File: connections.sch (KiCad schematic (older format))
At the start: 1 part

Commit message: Updated the schematic with some BUSes
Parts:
- added uUSB?: MICROUSB, symbol MICROUSB
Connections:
- net labels added: +5V, GNDPWR, USB0_0, USB0_1, USB0_2, eth0_0, eth0_1, eth0_10, eth0_2, eth0_3, eth0_4, eth0_5, eth0_6, eth0_7, eth0_8, eth0_9
- wire segments 0 -> 14
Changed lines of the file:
@@
-EESchema Schematic File Version 2  date 9/17/2011 12:57:37 AM
+EESchema Schematic File Version 2  date 9/17/2011 1:33:24 AM
 LIBS:power
 LIBS:device
@@
 LIBS:valves
 LIBS:rrae
+LIBS:connections-cache
 EELAYER 25  0
 EELAYER END
@@
 $EndDescr
 $Comp
+L GNDPWR #PWR?
+U 1 1 4E743F0C
+P 9800 2100
+F 0 "#PWR?" H 9800 2150 40  0001 C CNN
+F 1 "GNDPWR" H 9800 2020 40  0000 C CNN
+	1    9800 2100
+	1    0    0    -1
+$EndComp
+Wire Bus Line
+	7750 2100 7750 1100
+Wire Bus Line
+	5000 1800 5000 1600
+Wire Wire Line
+	5550 1700 5100 1700
+Wire Wire Line
+	5550 1800 5100 1800
+Wire Wire Line
+	5550 1900 5100 1900
+Wire Wire Line
+	8100 1200 7850 1200
+Wire Wire Line
+	8100 1300 7850 1300
+Wire Wire Line
+	8100 1400 7850 1400
+Wire Wire Line
+	8100 1500 7850 1500
+Wire Wire Line
+	8100 1600 7850 1600
+Wire Wire Line
+	8100 1700 7850 1700
+Wire Wire Line
+	8100 1800 7850 1800
+Wire Wire Line
+	8100 1900 7850 1900
+Wire Wire Line
+	8100 2000 7850 2000
+Wire Wire Line
+	8100 2100 7850 2100
+Wire Wire Line
+	8100 2200 7850 2200
+Entry Wire Line
+	7750 2100 7850 2200
+Entry Wire Line
+	7750 2000 7850 2100
+Entry Wire Line
+	7750 1900 7850 2000
+Entry Wire Line
+	7750 1800 7850 1900
+Entry Wire Line
+	7750 1700 7850 1800
+Entry Wire Line
+	7750 1600 7850 1700
+Entry Wire Line
+	7750 1500 7850 1600
+Entry Wire Line
+	7750 1400 7850 1500
+Entry Wire Line
+	7750 1300 7850 1400
+Entry Wire Line
+	7750 1200 7850 1300
+Entry Wire Line
+	7750 1100 7850 1200
+Text Label 7850 2200 0    60   ~ 0
+eth0_10
+Text Label 7850 2100 0    60   ~ 0
+eth0_9
+Text Label 7850 2000 0    60   ~ 0
+eth0_8
+Text Label 7850 1900 0    60   ~ 0
+eth0_7
+Text Label 7850 1800 0    60   ~ 0
+eth0_6
+Text Label 7850 1700 0    60   ~ 0
+eth0_5
+Text Label 7850 1600 0    60   ~ 0
+eth0_4
+Text Label 7850 1500 0    60   ~ 0
+eth0_3
+Text Label 7850 1400 0    60   ~ 0
+eth0_2
+Text Label 7850 1300 0    60   ~ 0
+eth0_1
+Text Label 7850 1200 0    60   ~ 0
+eth0_0
+Entry Wire Line
+	5000 1800 5100 1900
+Entry Wire Line
+	5000 1700 5100 1800
+Entry Wire Line
+	5000 1600 5100 1700
+Text Label 5100 1900 0    60   ~ 0
+USB0_2
+Text Label 5100 1800 0    60   ~ 0
+USB0_1
+Text Label 5100 1700 0    60   ~ 0
+USB0_0
+$Comp
+L +5V #PWR?
+U 1 1 4E743DEE
+P 5550 1600
+F 0 "#PWR?" H 5550 1690 20  0001 C CNN
+F 1 "+5V" H 5550 1690 30  0000 C CNN
+	1    5550 1600
+	1    0    0    -1
+$EndComp
+$Comp
+L GNDPWR #PWR?
+U 1 1 4E743D61
+P 5550 2000
+F 0 "#PWR?" H 5550 2050 40  0001 C CNN
+F 1 "GNDPWR" H 5550 1920 40  0000 C CNN
+	1    5550 2000
+	1    0    0    -1
+$EndComp
+$Comp
+L GNDPWR #PWR?
+U 1 1 4E743D59
+P 7050 1800
+F 0 "#PWR?" H 7050 1850 40  0001 C CNN
+F 1 "GNDPWR" H 7050 1720 40  0000 C CNN
+	1    7050 1800
+	1    0    0    -1
+$EndComp
+$Comp
+L MICROUSB uUSB?
+U 1 1 4E743BB6
+P 6300 1800
+F 0 "uUSB?" H 6300 2150 50  0000 C CNN
+F 1 "MICROUSB" H 6500 1600 50  0000 C CNN
+	1    6300 1800
+	1    0    0    -1
+$EndComp
+$Comp
 L RJ45-TRANSFO J?

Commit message: Made quite a few changes... The Eth Phy and RJ-45 connection should be close to finished. Figured out how to make the hierarchical sheets work.
Need to move the power schematic to a hierarchical sheet.
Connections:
- net labels added: DGND, Phy_LedGreen+, Phy_LedGreen-, Phy_recv+, Phy_recv-, Phy_trans+, Phy_trans-
- net labels removed: USB0_0, USB0_1, USB0_2, eth0_0, eth0_1, eth0_10, eth0_2, eth0_3, eth0_4, eth0_5, eth0_6, eth0_7, eth0_8, eth0_9
- wire segments 14 -> 0
- no-connect marks 0 -> 6
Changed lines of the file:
@@
-EESchema Schematic File Version 2  date 9/17/2011 1:33:24 AM
+EESchema Schematic File Version 2  date 9/24/2011 1:49:25 PM
 LIBS:power
 LIBS:device
@@
 LIBS:valves
 LIBS:rrae
-LIBS:connections-cache
+LIBS:rrae-cache
 EELAYER 25  0
 EELAYER END
 $Descr A4 11700 8267
 encoding utf-8
-Sheet 1 1
+Sheet 3 5
 Title "noname.sch"
-Date "17 sep 2011"
+Date "24 sep 2011"
 Rev ""
 Comp ""
@@
 Comment4 ""
 $EndDescr
+NoConn ~ 8100 2200
+NoConn ~ 8100 2100
+Text HLabel 8100 2000 0    60   Output ~ 0
+Phy_LedGreen-
+Text HLabel 8100 1900 0    60   Input ~ 0
+Phy_LedGreen+
+$Comp
+L DGND #PWR?
+U 1 1 4E7E1857
+P 8100 1800
+F 0 "#PWR?" H 8100 1800 40  0001 C CNN
+F 1 "DGND" H 8100 1730 40  0000 C CNN
+	1    8100 1800
+	0    1    1    0
+$EndComp
+NoConn ~ 8100 1600
+NoConn ~ 8100 1600
+NoConn ~ 8100 1300
+NoConn ~ 8100 1300
+Text HLabel 8100 1700 0    60   BiDi ~ 0
+Phy_recv-
+Text HLabel 8100 1500 0    60   BiDi ~ 0
+Phy_recv+
+Text HLabel 8100 1400 0    60   BiDi ~ 0
+Phy_trans-
+Text HLabel 8100 1200 0    60   BiDi ~ 0
+Phy_trans+
 $Comp
 L GNDPWR #PWR?
@@
 	1    0    0    -1
 $EndComp
-Wire Bus Line
-	7750 2100 7750 1100
-Wire Bus Line
-	5000 1800 5000 1600
-Wire Wire Line
-	5550 1700 5100 1700
-Wire Wire Line
-	5550 1800 5100 1800
-Wire Wire Line
-	5550 1900 5100 1900
-Wire Wire Line
-	8100 1200 7850 1200
-Wire Wire Line
-	8100 1300 7850 1300
-Wire Wire Line
-	8100 1400 7850 1400
-Wire Wire Line
-	8100 1500 7850 1500
-Wire Wire Line
-	8100 1600 7850 1600
-Wire Wire Line
-	8100 1700 7850 1700
-Wire Wire Line
-	8100 1800 7850 1800
-Wire Wire Line
-	8100 1900 7850 1900
-Wire Wire Line
-	8100 2000 7850 2000
-Wire Wire Line
-	8100 2100 7850 2100
-Wire Wire Line
-	8100 2200 7850 2200
-Entry Wire Line
-	7750 2100 7850 2200
-Entry Wire Line
-	7750 2000 7850 2100
-Entry Wire Line
-	7750 1900 7850 2000
-Entry Wire Line
-	7750 1800 7850 1900
-Entry Wire Line
-	7750 1700 7850 1800
-Entry Wire Line
-	7750 1600 7850 1700
-Entry Wire Line
-	7750 1500 7850 1600
-Entry Wire Line
-	7750 1400 7850 1500
-Entry Wire Line
-	7750 1300 7850 1400
-Entry Wire Line
-	7750 1200 7850 1300
-Entry Wire Line
-	7750 1100 7850 1200
-Text Label 7850 2200 0    60   ~ 0
-eth0_10
-Text Label 7850 2100 0    60   ~ 0
-eth0_9
-Text Label 7850 2000 0    60   ~ 0
-eth0_8
-Text Label 7850 1900 0    60   ~ 0
-eth0_7
-Text Label 7850 1800 0    60   ~ 0
-eth0_6
-Text Label 7850 1700 0    60   ~ 0
-eth0_5
-Text Label 7850 1600 0    60   ~ 0
-eth0_4
-Text Label 7850 1500 0    60   ~ 0
-eth0_3
-Text Label 7850 1400 0    60   ~ 0
-eth0_2
-Text Label 7850 1300 0    60   ~ 0
-eth0_1
-Text Label 7850 1200 0    60   ~ 0
-eth0_0
-Entry Wire Line
-	5000 1800 5100 1900
-Entry Wire Line
-	5000 1700 5100 1800
-Entry Wire Line
-	5000 1600 5100 1700
-Text Label 5100 1900 0    60   ~ 0
-USB0_2
-Text Label 5100 1800 0    60   ~ 0
-USB0_1
-Text Label 5100 1700 0    60   ~ 0
-USB0_0
 $Comp
 L +5V #PWR?

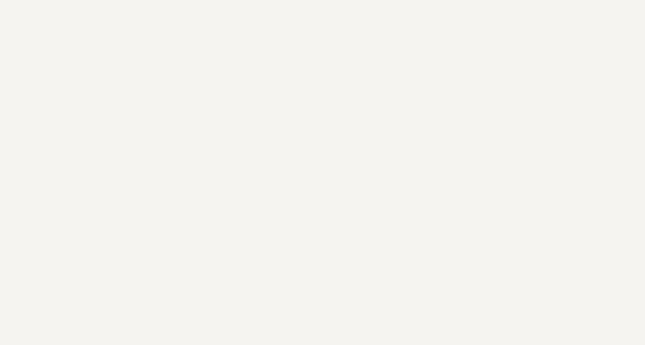
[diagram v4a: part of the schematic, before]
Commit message: Just added the uSD card to the schematic and connected it to the processor
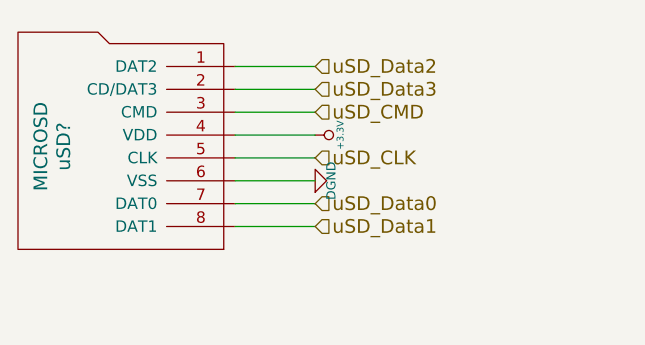
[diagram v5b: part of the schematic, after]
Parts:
- added uSD?: MICROSD, symbol MICROSD
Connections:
- net labels added: +3.3V, uSD_CLK, uSD_CMD, uSD_Data0, uSD_Data1, uSD_Data2, uSD_Data3
- wire segments 0 -> 8
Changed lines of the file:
@@
-EESchema Schematic File Version 2  date 9/26/2011 8:30:03 PM
+EESchema Schematic File Version 2  date 9/26/2011 11:46:43 PM
 LIBS:power
 LIBS:device
@@
 $Descr A4 11700 8267
 encoding utf-8
-Sheet 3 4
+Sheet 3 5
 Title "noname.sch"
 Date "27 sep 2011"
@@
 Comment4 ""
 $EndDescr
+Text HLabel 3950 1950 2    60   Input ~ 0
+uSD_Data1
+Text HLabel 3950 1850 2    60   Input ~ 0
+uSD_Data0
+$Comp
+L DGND #PWR?
+U 1 1 4E8152D9
+P 3950 1750
+F 0 "#PWR?" H 3950 1750 40  0001 C CNN
+F 1 "DGND" H 3950 1680 40  0000 C CNN
+	1    3950 1750
+	0    -1   -1   0
+$EndComp
+Text HLabel 3950 1650 2    60   Input ~ 0
+uSD_CLK
+$Comp
+L +3.3V #PWR?
+U 1 1 4E8152C3
+P 3950 1550
+F 0 "#PWR?" H 3950 1510 30  0001 C CNN
+F 1 "+3.3V" H 3950 1660 30  0000 C CNN
+	1    3950 1550
+	0    1    1    0
+$EndComp
+Text HLabel 3950 1450 2    60   Input ~ 0
+uSD_CMD
+Text HLabel 3950 1350 2    60   Input ~ 0
+uSD_Data3
+Text HLabel 3950 1250 2    60   Input ~ 0
+uSD_Data2
+Wire Wire Line
+	3600 1950 3950 1950
+Wire Wire Line
+	3600 1850 3950 1850
+Wire Wire Line
+	3600 1750 3950 1750
+Wire Wire Line
+	3600 1650 3950 1650
+Wire Wire Line
+	3600 1550 3950 1550
+Wire Wire Line
+	3600 1450 3950 1450
+Wire Wire Line
+	3600 1350 3950 1350
+Wire Wire Line
+	3600 1250 3950 1250
+$Comp
+L MICROSD uSD?
+U 1 1 4E815102
+P 3000 1600
+F 0 "uSD?" H 3000 1450 60  0000 C CNN
+F 1 "MICROSD" H 3000 1350 60  0000 C CNN
+	1    3000 1600
+	0    1    1    0
+$EndComp
 NoConn ~ 8100 2200
 NoConn ~ 8100 2100

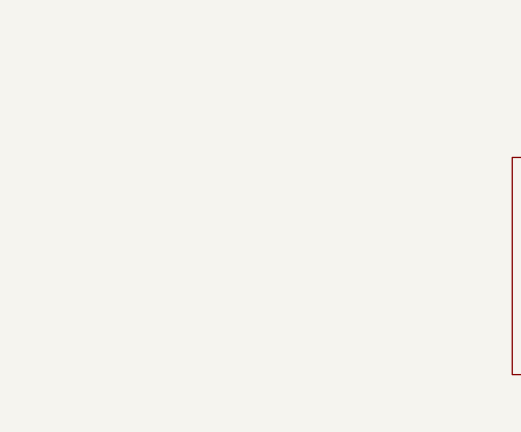
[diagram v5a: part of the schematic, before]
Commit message: Created the reset scheatic and connected it.  Still need to find a pin to do the soft reset.
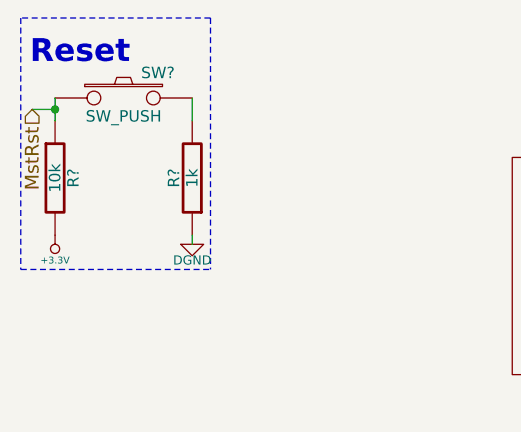
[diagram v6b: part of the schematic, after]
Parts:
- added R?: 10k, symbol R
- added R?: 1k, symbol R
- added SW?: SW_PUSH, symbol SW_PUSH
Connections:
- net labels added: MstRst
- wire segments 8 -> 12
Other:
- note added: "Reset"
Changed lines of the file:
@@
-EESchema Schematic File Version 2  date 9/26/2011 11:46:43 PM
+EESchema Schematic File Version 2  date 9/27/2011 12:42:11 AM
 LIBS:power
 LIBS:device
@@
 $Descr A4 11700 8267
 encoding utf-8
-Sheet 3 5
+Sheet 3 7
 Title "noname.sch"
 Date "27 sep 2011"
@@
 Comment4 ""
 $EndDescr
+Wire Wire Line
+	1250 1480 1250 1440
+Connection ~ 650  890
+Wire Wire Line
+	550  890  650  890
+Wire Wire Line
+	650  840  650  940
+Wire Wire Line
+	3600 1250 3950 1250
+Wire Wire Line
+	3600 1350 3950 1350
+Wire Wire Line
+	3600 1450 3950 1450
+Wire Wire Line
+	3600 1550 3950 1550
+Wire Wire Line
+	3600 1650 3950 1650
+Wire Wire Line
+	3600 1750 3950 1750
+Wire Wire Line
+	3600 1850 3950 1850
+Wire Wire Line
+	3600 1950 3950 1950
+Wire Wire Line
+	1250 940  1250 840
+Wire Notes Line
+	1330 490  1330 1590
+Wire Notes Line
+	1330 490  500  490
+Wire Notes Line
+	500  490  500  1590
+Wire Notes Line
+	500  1590 1330 1590
+Text Notes 540  700  0    100  ~ 20
+Reset
+$Comp
+L +3.3V #PWR?
+U 1 1 4E815BB9
+P 650 1440
+AR Path="/4E8158D9/4E815BB9" Ref="#PWR?"  Part="1"
+AR Path="/4E7A8C23/4E7E0D6B/4E815BB9" Ref="#PWR?"  Part="1"
+AR Path="/4E815C62/4E815C93/4E815BB9" Ref="#PWR?"  Part="1"
+F 0 "#PWR?" H 650 1400 30  0001 C CNN
+F 1 "+3.3V" H 650 1550 30  0000 C CNN
+	1    650  1440
+	-1   0    0    1
+$EndComp
+$Comp
+L SW_PUSH SW?
+U 1 1 4E815A3B
+P 950 840
+AR Path="/4E8158D9/4E815A3B" Ref="SW?"  Part="1"
+AR Path="/4E7A8C23/4E7E0D6B/4E815A3B" Ref="SW?"  Part="1"
+AR Path="/4E815C62/4E815C93/4E815A3B" Ref="SW?"  Part="1"
+F 0 "SW?" H 1100 950 50  0000 C CNN
+F 1 "SW_PUSH" H 950 760 50  0000 C CNN
+	1    950  840
+	1    0    0    -1
+$EndComp
+$Comp
+L R R?
+U 1 1 4E815B81
+P 1250 1190
+AR Path="/4E8158D9/4E815B81" Ref="R?"  Part="1"
+AR Path="/4E7A8C23/4E7E0D6B/4E815B81" Ref="R?"  Part="1"
+AR Path="/4E815C62/4E815C93/4E815B81" Ref="R?"  Part="1"
+F 0 "R?" V 1330 1190 50  0000 C CNN
+F 1 "1k" V 1250 1190 50  0000 C CNN
+	1    1250 1190
+	-1   0    0    1
+$EndComp
+$Comp
+L R R?
+U 1 1 4E815AE8
+P 650 1190
+AR Path="/4E8158D9/4E815AE8" Ref="R?"  Part="1"
+AR Path="/4E7A8C23/4E7E0D6B/4E815AE8" Ref="R?"  Part="1"
+AR Path="/4E815C62/4E815C93/4E815AE8" Ref="R?"  Part="1"
+F 0 "R?" V 730 1190 50  0000 C CNN
+F 1 "10k" V 650 1190 50  0000 C CNN
+	1    650  1190
+	1    0    0    -1
+$EndComp
+Text HLabel 550  890  3    60   Input ~ 0
+MstRst
+$Comp
+L DGND #PWR?
+U 1 1 4E815A9A
+P 1250 1480
+AR Path="/4E8158D9/4E815A9A" Ref="#PWR?"  Part="1"
+AR Path="/4E7A8C23/4E7E0D6B/4E815A9A" Ref="#PWR?"  Part="1"
+AR Path="/4E815C62/4E815C93/4E815A9A" Ref="#PWR?"  Part="1"
+F 0 "#PWR?" H 1250 1480 40  0001 C CNN
+F 1 "DGND" H 1250 1410 40  0000 C CNN
+	1    1250 1480
+	1    0    0    -1
+$EndComp
 Text HLabel 3950 1950 2    60   Input ~ 0
 uSD_Data1
@@
 U 1 1 4E8152D9
 P 3950 1750
+AR Path="/4E7A8C23/4E7E0D6B/4E8152D9" Ref="#PWR?"  Part="1"
+AR Path="/4E7DF058/4E815305/4E8152D9" Ref="#PWR?"  Part="1"
+AR Path="/4E8158D9/4E8152D9" Ref="#PWR?"  Part="1"
+AR Path="/4E815C62/4E815C93/4E8152D9" Ref="#PWR?"  Part="1"
 F 0 "#PWR?" H 3950 1750 40  0001 C CNN
 F 1 "DGND" H 3950 1680 40  0000 C CNN
@@
 U 1 1 4E8152C3
 P 3950 1550
+AR Path="/4E7A8C23/4E7E0D6B/4E8152C3" Ref="#PWR?"  Part="1"
+AR Path="/4E7DF058/4E815305/4E8152C3" Ref="#PWR?"  Part="1"
+AR Path="/4E8158D9/4E8152C3" Ref="#PWR?"  Part="1"
+AR Path="/4E815C62/4E815C93/4E8152C3" Ref="#PWR?"  Part="1"
 F 0 "#PWR?" H 3950 1510 30  0001 C CNN
 F 1 "+3.3V" H 3950 1660 30  0000 C CNN
@@
 Text HLabel 3950 1250 2    60   Input ~ 0
 uSD_Data2
-Wire Wire Line
-	3600 1950 3950 1950
-Wire Wire Line
-	3600 1850 3950 1850
-Wire Wire Line
-	3600 1750 3950 1750
-Wire Wire Line
-	3600 1650 3950 1650
-Wire Wire Line
-	3600 1550 3950 1550
-Wire Wire Line
-	3600 1450 3950 1450
-Wire Wire Line
-	3600 1350 3950 1350
-Wire Wire Line
-	3600 1250 3950 1250
 $Comp
 L MICROSD uSD?
 U 1 1 4E815102
 P 3000 1600
+AR Path="/4E7A8C23/4E7E0D6B/4E815102" Ref="uSD?"  Part="1"
+AR Path="/4E7DF058/4E815305/4E815102" Ref="uSD?"  Part="1"
+AR Path="/4E8158D9/4E815102" Ref="uSD?"  Part="1"
+AR Path="/4E815C62/4E815C93/4E815102" Ref="uSD?"  Part="1"
 F 0 "uSD?" H 3000 1450 60  0000 C CNN
 F 1 "MICROSD" H 3000 1350 60  0000 C CNN
@@
 U 1 1 4E7E1857
 P 8100 1800
+AR Path="/4E7A8C23/4E7E0D6B/4E7E1857" Ref="#PWR?"  Part="1"
+AR Path="/4E7DF058/4E815305/4E7E1857" Ref="#PWR?"  Part="1"
+AR Path="/4E8158D9/4E7E1857" Ref="#PWR?"  Part="1"
+AR Path="/4E815C62/4E815C93/4E7E1857" Ref="#PWR?"  Part="1"
 F 0 "#PWR?" H 8100 1800 40  0001 C CNN
 F 1 "DGND" H 8100 1730 40  0000 C CNN
@@
 U 1 1 4E743F0C
 P 9800 2100
+AR Path="/4E7A8C23/4E7E0D6B/4E743F0C" Ref="#PWR?"  Part="1"
+AR Path="/4E7DF058/4E815305/4E743F0C" Ref="#PWR?"  Part="1"
+AR Path="/4E8158D9/4E743F0C" Ref="#PWR?"  Part="1"
+AR Path="/4E815C62/4E815C93/4E743F0C" Ref="#PWR?"  Part="1"
 F 0 "#PWR?" H 9800 2150 40  0001 C CNN
 F 1 "GNDPWR" H 9800 2020 40  0000 C CNN
@@
 U 1 1 4E743DEE
 P 5550 1600
+AR Path="/4E7A8C23/4E7E0D6B/4E743DEE" Ref="#PWR?"  Part="1"
+AR Path="/4E7DF058/4E815305/4E743DEE" Ref="#PWR?"  Part="1"
+AR Path="/4E8158D9/4E743DEE" Ref="#PWR?"  Part="1"
+AR Path="/4E815C62/4E815C93/4E743DEE" Ref="#PWR?"  Part="1"
 F 0 "#PWR?" H 5550 1690 20  0001 C CNN
 F 1 "+5V" H 5550 1690 30  0000 C CNN
@@
 U 1 1 4E743D61
 P 5550 2000
+AR Path="/4E7A8C23/4E7E0D6B/4E743D61" Ref="#PWR?"  Part="1"
+AR Path="/4E7DF058/4E815305/4E743D61" Ref="#PWR?"  Part="1"
+AR Path="/4E8158D9/4E743D61" Ref="#PWR?"  Part="1"
+AR Path="/4E815C62/4E815C93/4E743D61" Ref="#PWR?"  Part="1"
 F 0 "#PWR?" H 5550 2050 40  0001 C CNN
 F 1 "GNDPWR" H 5550 1920 40  0000 C CNN
@@
 U 1 1 4E743D59
 P 7050 1800
+AR Path="/4E7A8C23/4E7E0D6B/4E743D59" Ref="#PWR?"  Part="1"
+AR Path="/4E7DF058/4E815305/4E743D59" Ref="#PWR?"  Part="1"
+AR Path="/4E8158D9/4E743D59" Ref="#PWR?"  Part="1"
+AR Path="/4E815C62/4E815C93/4E743D59" Ref="#PWR?"  Part="1"
 F 0 "#PWR?" H 7050 1850 40  0001 C CNN
 F 1 "GNDPWR" H 7050 1720 40  0000 C CNN
@@
 U 1 1 4E743BB6
 P 6300 1800
+AR Path="/4E7A8C23/4E7E0D6B/4E743BB6" Ref="uUSB?"  Part="1"
+AR Path="/4E7DF058/4E815305/4E743BB6" Ref="uUSB?"  Part="1"
+AR Path="/4E8158D9/4E743BB6" Ref="uUSB?"  Part="1"
+AR Path="/4E815C62/4E815C93/4E743BB6" Ref="uUSB?"  Part="1"
 F 0 "uUSB?" H 6300 2150 50  0000 C CNN
 F 1 "MICROUSB" H 6500 1600 50  0000 C CNN
@@
 U 1 1 4E741312
 P 9200 1700
+AR Path="/4E7A8C23/4E7E0D6B/4E741312" Ref="J?"  Part="1"
+AR Path="/4E7DF058/4E815305/4E741312" Ref="J?"  Part="1"
+AR Path="/4E8158D9/4E741312" Ref="J?"  Part="1"
+AR Path="/4E815C62/4E815C93/4E741312" Ref="J?"  Part="1"
 F 0 "J?" H 9300 2300 60  0000 L CNN
 F 1 "RJ45-TRANSFO" H 9150 2300 60  0000 R CNN
